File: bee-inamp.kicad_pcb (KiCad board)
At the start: 2 copper layers, 13.7 x 53.3 mm, 15 parts, among them J1 Conn_01x02_Male, J2 Conn_01x02_Male, J3 Conn_01x02_Male, J4 Conn_01x02_Male, J5 Conn_01x02, J6 Conn_01x02, J7 Conn_02x03_Odd_Even, J8 Conn_01x03, J9 Conn_01x02, U1 INA126

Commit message: Add labels for G.
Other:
- board text added: "G var."
- board text added: "G=10"
- board text added: "G=100"
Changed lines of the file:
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@@
   (general
     (thickness 1.6)
-    (drawings 4)
+    (drawings 13)
     (tracks 89)
     (zones 0)
@@
     (descr "Through hole straight socket strip, 1x02, 2.54mm pitch, single row (from Kicad 4.0.7), script generated")
     (tags "Through hole socket strip THT 1x02 2.54mm single row")
-    (fp_text reference J6 (at -2.159 3.302 90) (layer F.SilkS)
+    (fp_text reference J6 (at -0.127 5.08 180) (layer F.SilkS)
       (effects (font (size 1 1) (thickness 0.15)))
     )
@@
     (descr "Through hole straight socket strip, 1x02, 2.54mm pitch, single row (from Kicad 4.0.7), script generated")
     (tags "Through hole socket strip THT 1x02 2.54mm single row")
-    (fp_text reference J5 (at -2.159 -0.762 90) (layer F.SilkS)
+    (fp_text reference J5 (at -0.127 4.572 180) (layer F.SilkS)
       (effects (font (size 1 1) (thickness 0.15)))
     )
@@
     )
   )
+  (gr_line (start 87.63 130.048) (end 87.63 117.602) (layer F.SilkS) (width 0.2))
+  (gr_line (start 81.28 130.048) (end 87.63 130.048) (layer F.SilkS) (width 0.2))
+  (gr_line (start 81.28 114.3) (end 81.28 130.048) (layer F.SilkS) (width 0.2))
+  (gr_line (start 83.566 114.3) (end 81.28 114.3) (layer F.SilkS) (width 0.2))
+  (gr_line (start 83.566 117.602) (end 83.566 114.3) (layer F.SilkS) (width 0.2))
+  (gr_line (start 87.63 117.602) (end 83.566 117.602) (layer F.SilkS) (width 0.2))
+  (gr_text "G var." (at 82.55 116.84 90) (layer F.SilkS)
+    (effects (font (size 1 1) (thickness 0.15)))
+  )
+  (gr_text G=100 (at 80.01 116.586 90) (layer F.SilkS)
+    (effects (font (size 1 1) (thickness 0.15)))
+  )
+  (gr_text G=10 (at 78.232 117.094 90) (layer F.SilkS)
+    (effects (font (size 1 1) (thickness 0.15)))
+  )
   (gr_line (start 88.138 88.9) (end 88.138 142.24) (layer Edge.Cuts) (width 0.15))

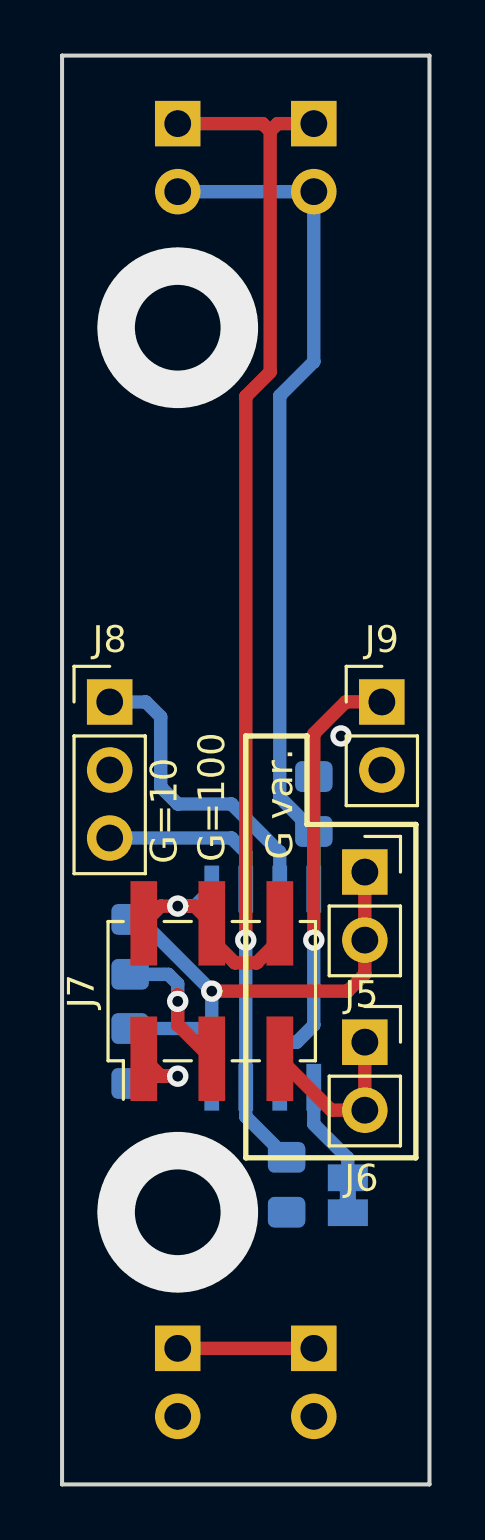
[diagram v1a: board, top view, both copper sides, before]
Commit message: Update labels and mounting holes.
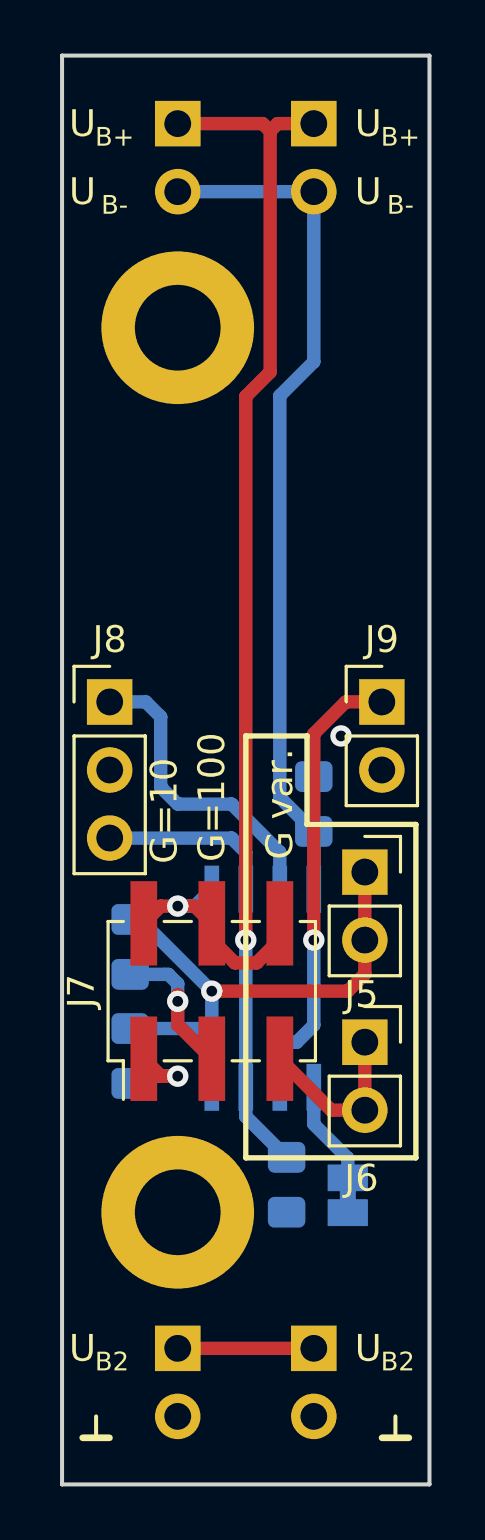
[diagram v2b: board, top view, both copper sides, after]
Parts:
- added H1: Silkscreen_Label, Symbol-emt:Text_U_B+_Silkscreen, F.Cu at (75.2, 91.4)
- added H10: MountingHole_Pad, MountingHole:MountingHole_3.2mm_M3_ISO7380_Pad, F.Cu at (78.7, 132.1)
- added H2: Silkscreen_Label, Symbol-emt:Text_U_B+_Silkscreen, F.Cu at (85.9, 91.4)
- added H3: Silkscreen_Label, Symbol-emt:Text_U_B-_Silkscreen, F.Cu at (75.2, 94.0)
- added H4: Silkscreen_Label, Symbol-emt:Text_U_B-_Silkscreen, F.Cu at (85.9, 94.0)
- added H5: Silkscreen_Label, Symbol-emt:Text_U_B2_Silkscreen, F.Cu at (75.2, 137.2)
- added H6: Silkscreen_Label, Symbol-emt:Text_U_B2_Silkscreen, F.Cu at (85.9, 137.2)
- added H7: Silkscreen_Label, Symbol-emt:Symbol_GND_Silkscreen, F.Cu at (75.7, 139.7)
- added H8: Silkscreen_Label, Symbol-emt:Symbol_GND_Silkscreen, F.Cu at (86.9, 139.7)
- added H9: MountingHole_Pad, MountingHole:MountingHole_3.2mm_M3_ISO7380_Pad, F.Cu at (78.7, 99.1)
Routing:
- net (no net): vias 2 -> 0
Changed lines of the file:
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@@
     (thickness 1.6)
     (drawings 13)
-    (tracks 89)
+    (tracks 87)
     (zones 0)
-    (modules 15)
+    (modules 25)
     (nets 14)
   )
@@
     )
   )
+  (module Symbol-emt:Text_U_B+_Silkscreen (layer F.Cu)
+    (at 75.184 91.44)
+    (descr "Voltage Label Betriebsspannung")
+    (tags "Voltage Label Betriebsspannung")
+    (attr virtual)
+    (fp_text reference H1 (at 0 1.65) (layer F.SilkS) hide
+      (effects (font (size 1 1) (thickness 0.15)))
+    )
+    (fp_text value Silkscreen_Label (at 0 -1.5) (layer F.Fab) hide
+      (effects (font (size 1 1) (thickness 0.15)))
+    )
+    (fp_text user B+ (at 1.2 0.5) (layer F.SilkS)
+      (effects (font (size 0.7 0.7) (thickness 0.1)))
+    )
+    (fp_text user U (at 0 0) (layer F.SilkS)
+      (effects (font (size 1 1) (thickness 0.15)))
+    )
+  )
+  (module Symbol-emt:Text_U_B+_Silkscreen (layer F.Cu)
+    (at 85.852 91.44)
+    (descr "Voltage Label Betriebsspannung")
+    (tags "Voltage Label Betriebsspannung")
+    (attr virtual)
+    (fp_text reference H2 (at 0 1.65) (layer F.SilkS) hide
+      (effects (font (size 1 1) (thickness 0.15)))
+    )
+    (fp_text value Silkscreen_Label (at 0 -1.5) (layer F.Fab) hide
+      (effects (font (size 1 1) (thickness 0.15)))
+    )
+    (fp_text user U (at 0 0) (layer F.SilkS)
+      (effects (font (size 1 1) (thickness 0.15)))
+    )
+    (fp_text user B+ (at 1.2 0.5) (layer F.SilkS)
+      (effects (font (size 0.7 0.7) (thickness 0.1)))
+    )
+  )
+  (module Symbol-emt:Text_U_B-_Silkscreen (layer F.Cu)
+    (at 75.184 93.98)
+    (descr "Voltage Label Betriebsspannung")
+    (tags "Voltage Label Betriebsspannung")
+    (attr virtual)
+    (fp_text reference H3 (at 0 1.65) (layer F.SilkS) hide
+      (effects (font (size 1 1) (thickness 0.15)))
+    )
+    (fp_text value Silkscreen_Label (at 0 -1.5) (layer F.Fab) hide
+      (effects (font (size 1 1) (thickness 0.15)))
+    )
+    (fp_text user B- (at 1.2 0.5) (layer F.SilkS)
+      (effects (font (size 0.7 0.7) (thickness 0.1)))
+    )
+    (fp_text user U (at 0 0) (layer F.SilkS)
+      (effects (font (size 1 1) (thickness 0.15)))
+    )
+  )
+  (module Symbol-emt:Text_U_B-_Silkscreen (layer F.Cu)
+    (at 85.852 93.98)
+    (descr "Voltage Label Betriebsspannung")
+    (tags "Voltage Label Betriebsspannung")
+    (attr virtual)
+    (fp_text reference H4 (at 0 1.65) (layer F.SilkS) hide
+      (effects (font (size 1 1) (thickness 0.15)))
+    )
+    (fp_text value Silkscreen_Label (at 0 -1.5) (layer F.Fab) hide
+      (effects (font (size 1 1) (thickness 0.15)))
+    )
+    (fp_text user U (at 0 0) (layer F.SilkS)
+      (effects (font (size 1 1) (thickness 0.15)))
+    )
+    (fp_text user B- (at 1.2 0.5) (layer F.SilkS)
+      (effects (font (size 0.7 0.7) (thickness 0.1)))
+    )
+  )
+  (module Symbol-emt:Text_U_B2_Silkscreen (layer F.Cu)
+    (at 75.184 137.16)
+    (descr "Voltage Label Betriebsspannung")
+    (tags "Voltage Label Betriebsspannung")
+    (attr virtual)
+    (fp_text reference H5 (at 0 1.65) (layer F.SilkS) hide
+      (effects (font (size 1 1) (thickness 0.15)))
+    )
+    (fp_text value Silkscreen_Label (at 0 -1.5) (layer F.Fab) hide
+      (effects (font (size 1 1) (thickness 0.15)))
+    )
+    (fp_text user B2 (at 1.1 0.5) (layer F.SilkS)
+      (effects (font (size 0.7 0.7) (thickness 0.1)))
+    )
+    (fp_text user U (at 0 0) (layer F.SilkS)
+      (effects (font (size 1 1) (thickness 0.15)))
+    )
+  )
+  (module Symbol-emt:Text_U_B2_Silkscreen (layer F.Cu)
+    (at 85.852 137.16)
+    (descr "Voltage Label Betriebsspannung")
+    (tags "Voltage Label Betriebsspannung")
+    (attr virtual)
+    (fp_text reference H6 (at 0 1.65) (layer F.SilkS) hide
+      (effects (font (size 1 1) (thickness 0.15)))
+    )
+    (fp_text value Silkscreen_Label (at 0 -1.5) (layer F.Fab) hide
+      (effects (font (size 1 1) (thickness 0.15)))
+    )
+    (fp_text user U (at 0 0) (layer F.SilkS)
+      (effects (font (size 1 1) (thickness 0.15)))
+    )
+    (fp_text user B2 (at 1.1 0.5) (layer F.SilkS)
+      (effects (font (size 0.7 0.7) (thickness 0.1)))
+    )
+  )
+  (module Symbol-emt:Symbol_GND_Silkscreen (layer F.Cu)
+    (at 75.692 139.7)
+    (descr "Symbol GND")
+    (tags "Symbol GND")
+    (attr virtual)
+    (fp_text reference H7 (at 0 1.6) (layer F.SilkS) hide
+      (effects (font (size 1 1) (thickness 0.15)))
+    )
+    (fp_text value Silkscreen_Label (at 0 -0.75) (layer F.Fab) hide
+      (effects (font (size 1 1) (thickness 0.15)))
+    )
+    (fp_line (start 0 0.8) (end 0 0) (layer F.SilkS) (width 0.15))
+    (fp_line (start -0.5 0.8) (end 0.5 0.8) (layer F.SilkS) (width 0.25))
+  )
+  (module Symbol-emt:Symbol_GND_Silkscreen (layer F.Cu)
+    (at 86.868 139.7)
+    (descr "Symbol GND")
+    (tags "Symbol GND")
+    (attr virtual)
+    (fp_text reference H8 (at 0 1.6) (layer F.SilkS) hide
+      (effects (font (size 1 1) (thickness 0.15)))
+    )
+    (fp_text value Silkscreen_Label (at 0 -0.75) (layer F.Fab) hide
+      (effects (font (size 1 1) (thickness 0.15)))
+    )
+    (fp_line (start -0.5 0.8) (end 0.5 0.8) (layer F.SilkS) (width 0.25))
+    (fp_line (start 0 0.8) (end 0 0) (layer F.SilkS) (width 0.15))
+  )
+  (module MountingHole:MountingHole_3.2mm_M3_ISO7380_Pad locked (layer F.Cu)
+    (at 78.74 99.06)
+    (descr "Mounting Hole 3.2mm, M3, ISO7380")
+    (tags "mounting hole 3.2mm m3 iso7380")
+    (attr virtual)
+    (fp_text reference H9 (at 0 -3.85) (layer F.SilkS) hide
+      (effects (font (size 1 1) (thickness 0.15)))
+    )
+    (fp_text value MountingHole_Pad (at 0 3.85) (layer F.Fab)
+      (effects (font (size 1 1) (thickness 0.15)))
+    )
+    (fp_circle (center 0 0) (end 3.1 0) (layer F.CrtYd) (width 0.05))
+    (fp_circle (center 0 0) (end 2.85 0) (layer Cmts.User) (width 0.15))
+    (fp_text user %R (at 0.3 0) (layer F.Fab)
+      (effects (font (size 1 1) (thickness 0.15)))
+    )
+    (pad 1 thru_hole circle (at 0 0) (size 5.7 5.7) (drill 3.2) (layers *.Cu *.Mask)
+      (net 3 GND))
+  )
+  (module MountingHole:MountingHole_3.2mm_M3_ISO7380_Pad locked (layer F.Cu)
+    (at 78.74 132.08)
+    (descr "Mounting Hole 3.2mm, M3, ISO7380")
+    (tags "mounting hole 3.2mm m3 iso7380")
+    (attr virtual)
+    (fp_text reference H10 (at 0 -3.85) (layer F.SilkS) hide
+      (effects (font (size 1 1) (thickness 0.15)))
+    )
+    (fp_text value MountingHole_Pad (at 0 3.85) (layer F.Fab)
+      (effects (font (size 1 1) (thickness 0.15)))
+    )
+    (fp_text user %R (at 0.3 0) (layer F.Fab)
+      (effects (font (size 1 1) (thickness 0.15)))
+    )
+    (fp_circle (center 0 0) (end 2.85 0) (layer Cmts.User) (width 0.15))
+    (fp_circle (center 0 0) (end 3.1 0) (layer F.CrtYd) (width 0.05))
+    (pad 1 thru_hole circle (at 0 0) (size 5.7 5.7) (drill 3.2) (layers *.Cu *.Mask)
+      (net 3 GND))
+  )
   (gr_line (start 87.63 130.048) (end 87.63 117.602) (layer F.SilkS) (width 0.2))
   (gr_line (start 81.28 130.048) (end 87.63 130.048) (layer F.SilkS) (width 0.2))
@@
   (gr_line (start 74.422 88.9) (end 88.138 88.9) (layer Edge.Cuts) (width 0.15))
   (gr_line (start 74.422 88.9) (end 74.422 142.24) (layer Edge.Cuts) (width 0.15))
-  (via (at 78.74 99.06) (size 6) (drill 3.2) (layers F.Cu B.Cu) (net 0) (status 40000))
-  (via (at 78.74 132.08) (size 6) (drill 3.2) (layers F.Cu B.Cu) (net 0) (status 40000))
   (segment (start 83.82 120.015) (end 83.82 117.865) (width 0.5) (layer B.Cu) (net 1))
   (segment (start 82.55 116.595) (end 82.55 101.6) (width 0.5) (layer B.Cu) (net 1))
